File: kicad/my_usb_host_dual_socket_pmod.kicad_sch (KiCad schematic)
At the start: 16 parts, among them J1 USB_A_Stacked, J2 Conn_02x06_Odd_Even, J3 Conn_01x02_Socket, U2 QX2303L50T

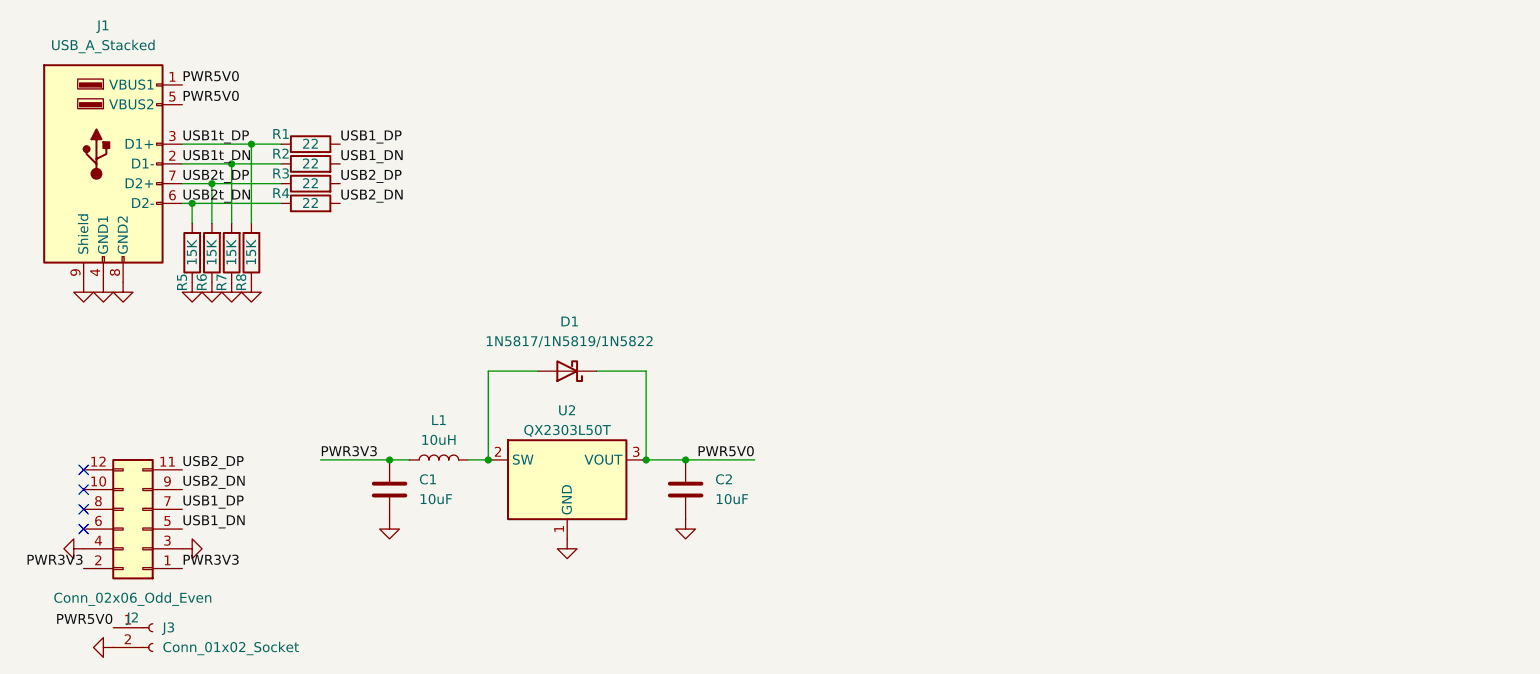
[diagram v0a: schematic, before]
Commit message: Changed 5V0 regulator to TPS61253A which supports more current
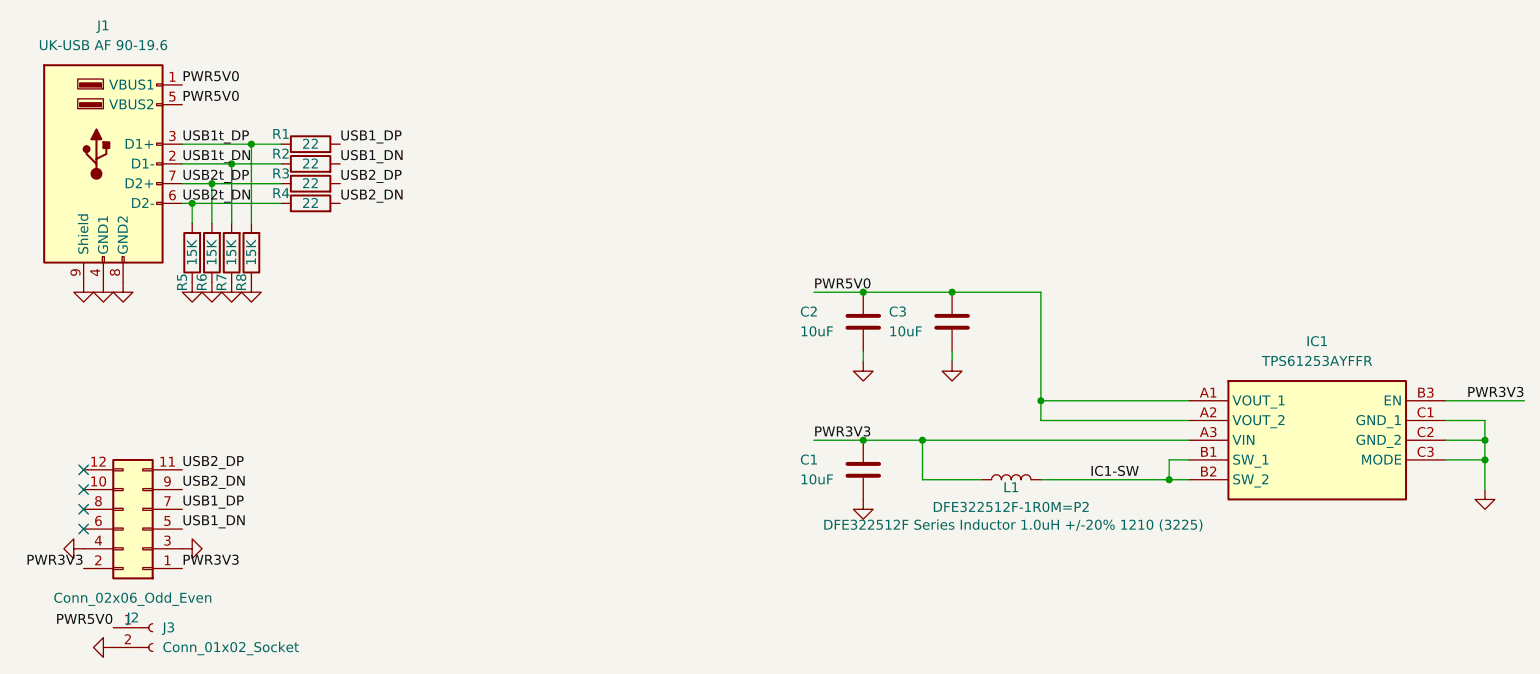
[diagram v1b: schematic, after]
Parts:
- removed D1: 1N5817/1N5819/1N5822, Diode_SMD:D_0402_1005Metric, symbol Diode:1N5822
- removed U2: QX2303L50T, Package_TO_SOT_SMD:SOT-23, symbol Regulator_Switching:TPS61322DBZ
- added C3: 10uF, Capacitor_SMD:C_0603_1608Metric, symbol Device:C
- added IC1: TPS61253AYFFR, libs:BGA9C40P3X3_119X129X62, symbol TPS61253AYFFR:TPS61253AYFFR
- C2: footprint Capacitor_SMD:C_0402_1005Metric -> Capacitor_SMD:C_0603_1608Metric
- J1: value USB_A_Stacked -> UK-USB AF 90-19.6
- L1: value 10uH -> DFE322512F-1R0M=P2; footprint Inductor_SMD:L_0603_1608Metric -> Inductor_SMD:L_1210_3225Metric
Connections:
- net GND: now also C3.2, IC1.C1 (GND_1), IC1.C2 (GND_2), IC1.C3 (MODE)
- net PWR3V3: now also IC1.A3 (VIN), IC1.B3 (EN)
- net PWR5V0: now also C3.1, IC1.A1 (VOUT_1), IC1.A2 (VOUT_2)
- net IC1-SW: now reaches L1.2
- net IC1-SW: now also IC1.B1 (SW_1), IC1.B2 (SW_2)
